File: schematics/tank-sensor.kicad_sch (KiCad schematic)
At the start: 32 parts, among them J10 Solar Panel, J8 Pressure Sensor, J9 Battery Connector, Q1 BS170, U1 ESP32-C6-DevKitC-1, U2 TSR_1-2450

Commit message: feat: Update component names
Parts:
- K1: value ~ -> EC2-12NU
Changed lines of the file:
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@@
 			)
 		)
-		(property "Value" "~"
+		(property "Value" "EC2-12NU"
 			(at 184.15 79.3496 90)
 			(effects

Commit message: feat: More updates to schematics
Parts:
- removed H1, H2, H3, H4: ~, symbol Mechanical:MountingHole
- removed U2: (no value), symbol AW_Misc_Library:Adafruit_ADS1115_Module
- removed U3: (no value), symbol AW_Misc_Library:XL6009E1_DC-DC_Stepup_Converter
- removed U4: (no value), symbol AW_Misc_Library:SDLA12TA_SLA_Charge_Module
- removed U5: (no value), symbol AW_Misc_Library:Pimoroni_BME280_Module
- added J11: SDLA12TA Charge module, symbol Connector_Generic:Conn_02x02_Counter_Clockwise
- added J12: XL6009E1 DC-DC converter, symbol Connector_Generic:Conn_01x04
- added U3: BME280, Package_LGA:Bosch_LGA-8_2.5x2.5mm_P0.65mm_ClockwisePinNumbering, symbol Sensor:BME280
- added U4: ADS1115, 1085:MODULE_1085, symbol 1085:1085
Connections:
- net 3v3: now also U4.JP2_1 (VIN)
- net BATTERY+12: now also J11.BAT
- net BATTLEVEL_SENSE: now also U4.JP1_5 (A0)
- net BOOST24POS: now also J12.3 (Pin_3)
- net BOOST_SUPPLY: now also J12.1 (IN_+)
- net GND: now also J11.GND, J12.2 (Pin_2), J12.4 (Pin_4), U3.1 (GND), U4.JP2_2 (GND)
- net LDR_SENSE: now also U4.JP1_3 (A2)
- net PANEL_NEG: now also J11.GND
- net PANEL_POS: now also J11.VIN
- net PRESS_SENSE: now also U4.JP1_4 (A1)
- net SCL: now also U4.JP2_3 (SCL)
- net SDA: now also U4.JP2_4 (SDA)
- new net: U4.SH1 (SHIELD), U4.SH2 (SHIELD), U4.SH3 (SHIELD), U4.SH4 (SHIELD)
- no-connect marks 11 -> 8
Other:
- note removed: "24V supply and sensing for submersible pressure sensor"
- note removed: "Analogue to Digital Conversion"
- note removed: "Environment Monitor and Control"
- note removed: "Power Supply"
- note removed: "Power control for 24V boost converter power supply"
- moved on the sheet: D1, D2, J1, J10, J2, J3, J4, J5, J6, J7, J8, J9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

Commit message: feat:Connected all the parts in the schematic
Almost complete, need to verify numbers for resistors
and diodes

#3
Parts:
- removed U3: BME280, Package_LGA:Bosch_LGA-8_2.5x2.5mm_P0.65mm_ClockwisePinNumbering, symbol Sensor:BME280
- added J13: BME280 3.3V, symbol Connector_Generic:Conn_01x06
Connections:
- net 3v3: now also U1.1 (3V3), J13.6 (Pin_6)
- net BATTLEVEL_SENSE: now also U4.JP1_2 (A3); no longer U4.JP1_5 (A0)
- net BOOST_ENABLE: now also U1.23 (GPIO18)
- net GND: now also J13.5 (Pin_5)
- net LDR_SENSE: now also U4.JP1_5 (A0); no longer U4.JP1_3 (A2)
- net OFFLINE_MODE: now also U1.28 (GPIO23)
- net SCL: now also U1.11 (GPIO11), J13.4 (Pin_4)
- net SDA: now also U1.10 (GPIO10), J13.3 (Pin_3)
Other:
- moved on the sheet: D1, R1, R2, R4, R7, SW1, U1, U4

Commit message: Just in case
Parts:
- removed D2: ~, symbol Device:D
- added D3: 1N4007, Diode_THT:D_DO-41_SOD81_P10.16mm_Horizontal, symbol Diode:1N4007
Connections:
- net BATTERY+12: now also D3.1 (K)
- net BOOST_SWITCH: now also D3.2 (A)
- no-connect marks 8 -> 38
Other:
- note added: "mosfet"
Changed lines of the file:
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@@
 	)
 	(no_connect
+		(at 63.5 97.79)
+	)
+	(no_connect
+		(at 33.02 90.17)
+	)
+	(no_connect
 		(at 73.66 30.48)
 	)
@@
 	)
 	(no_connect
+		(at 137.16 124.46)
+	)
+	(no_connect
+		(at 63.5 105.41)
+	)
+	(no_connect
+		(at 137.16 144.78)
+	)
+	(no_connect
+		(at 86.36 129.54)
+	)
+	(no_connect
 		(at 261.62 72.39)
 	)
 	(no_connect
+		(at 33.02 95.25)
+	)
+	(no_connect
+		(at 137.16 129.54)
+	)
+	(no_connect
+		(at 86.36 132.08)
+	)
+	(no_connect
+		(at 137.16 127)
+	)
+	(no_connect
+		(at 137.16 142.24)
+	)
+	(no_connect
+		(at 86.36 154.94)
+	)
+	(no_connect
+		(at 137.16 134.62)
+	)
+	(no_connect
+		(at 137.16 132.08)
+	)
+	(no_connect
+		(at 137.16 157.48)
+	)
+	(no_connect
+		(at 33.02 102.87)
+	)
+	(no_connect
+		(at 86.36 147.32)
+	)
+	(no_connect
+		(at 82.55 177.8)
+	)
+	(no_connect
+		(at 86.36 144.78)
+	)
+	(no_connect
 		(at 161.29 35.56)
 	)
 	(no_connect
+		(at 82.55 180.34)
+	)
+	(no_connect
+		(at 86.36 139.7)
+	)
+	(no_connect
+		(at 137.16 154.94)
+	)
+	(no_connect
+		(at 86.36 152.4)
+	)
+	(no_connect
 		(at 261.62 69.85)
 	)
 	(no_connect
+		(at 86.36 124.46)
+	)
+	(no_connect
 		(at 31.75 22.86)
 	)
 	(no_connect
+		(at 86.36 142.24)
+	)
+	(no_connect
+		(at 44.45 22.86)
+	)
+	(no_connect
+		(at 63.5 92.71)
+	)
+	(no_connect
 		(at 161.29 25.4)
 	)
 	(no_connect
-		(at 46.99 20.32)
+		(at 86.36 149.86)
+	)
+	(no_connect
+		(at 137.16 139.7)
+	)
+	(no_connect
+		(at 137.16 152.4)
+	)
+	(no_connect
+		(at 137.16 147.32)
 	)
 	(wire
@@
 	(wire
 		(pts
-			(xy 172.72 55.88) (xy 179.07 55.88)
+			(xy 172.72 59.69) (xy 179.07 59.69)
 		)
 		(stroke
@@
 	(wire
 		(pts
-			(xy 158.75 43.18) (xy 158.75 55.88)
+			(xy 158.75 43.18) (xy 158.75 59.69)
 		)
 		(stroke
@@
 	(wire
 		(pts
-			(xy 158.75 55.88) (xy 165.1 55.88)
+			(xy 158.75 59.69) (xy 165.1 59.69)
 		)
 		(stroke
@@
 	(wire
 		(pts
-			(xy 179.07 55.88) (xy 179.07 43.18)
+			(xy 179.07 59.69) (xy 179.07 43.18)
 		)
 		(stroke
@@
 		)
 	)
+	(text "mosfet"
+		(exclude_from_sim no)
+		(at 189.23 79.756 0)
+		(effects
+			(font
+				(size 1.27 1.27)
+			)
+		)
+	)
 	(text "This is intended as a green LED\n with 2V drop and 15mA."
 		(exclude_from_sim no)
@@
 		)
 	)
-	(global_label "3v3"
-		(shape input)
-		(at 127 176.53 180)
-		(fields_autoplaced yes)
-		(effects
-			(font
-				(size 1.27 1.27)
-			)
-			(justify right)
-		)
-		(property "Intersheetrefs" "${INTERSHEET_REFS}"
-			(at 120.6282 176.53 0)
-			(effects
-				(font
-					(size 1.27 1.27)
-				)
-				(justify right)
-				(hide yes)
-			)
-		)
-	)
 	(global_label "BATTERY+12"
 		(shape input)
@@
 	(global_label "CONSOLE_RX"
 		(shape input)
-		(at 168.91 118.11 0)
+		(at 171.45 125.73 0)
 		(fields_autoplaced yes)
 		(effects
@@
 		)
 		(property "Intersheetrefs" "${INTERSHEET_REFS}"
-			(at 183.9904 118.11 0)
+			(at 186.5304 125.73 0)
 			(effects
 				(font
@@
 		(dnp no)
 		(property "Reference" "K1"
-			(at 168.91 52.5018 90)
+			(at 169.164 14.224 90)
 			(effects
 				(font
@@
 		)
 		(property "Value" "EC2-12NU"
-			(at 168.91 50.1904 90)
+			(at 168.91 16.256 90)
 			(effects
 				(font
@@
 	)
 	(symbol
-		(lib_id "Device:D")
-		(at 168.91 55.88 0)
-		(unit 1)
-		(exclude_from_sim no)
-		(in_bom yes)
-		(on_board yes)
-		(dnp no)
-		(property "Reference" "D2"
-			(at 168.91 61.3918 0)
-			(effects
-				(font
-					(size 1.27 1.27)
-				)
-			)
-		)
-		(property "Value" "~"
-			(at 168.91 59.0804 0)
-			(effects
-				(font
-					(size 1.27 1.27)
-				)
-			)
-		)
-		(property "Footprint" ""
-			(at 168.91 55.88 0)
-			(effects
-				(font
-					(size 1.27 1.27)
-				)
-				(hide yes)
-			)
-		)
-		(property "Datasheet" "~"
-			(at 168.91 55.88 0)
-			(effects
-				(font
-					(size 1.27 1.27)
-				)
-				(hide yes)
-			)
-		)
-		(property "Description" ""
-			(at 168.91 55.88 0)
-			(effects
-				(font
-					(size 1.27 1.27)
-				)
-				(hide yes)
-			)
-		)
-		(pin "1"
-		)
-		(pin "2"
-		)
-		(instances
-			(project "tank-sensor"
-				(path "/a113f251-aa94-483d-8b1b-4a797e2f25c2"
-					(reference "D2")
-					(unit 1)
-				)
-			)
-		)
-	)
-	(symbol
 		(lib_id "power:GND")
 		(at 25.4 129.54 180)
@@
 					(unit 1)
 				)
+			)
+		)
+	)
+	(symbol
+		(lib_id "Diode:1N4007")
+		(at 168.91 59.69 0)
+		(unit 1)
+		(exclude_from_sim no)
+		(in_bom yes)
+		(on_board yes)
+		(dnp no)
+		(fields_autoplaced yes)
+		(property "Reference" "D3"
+			(at 168.91 53.34 0)
+			(effects
+				(font
+					(size 1.27 1.27)
+				)
+			)
+		)
+		(property "Value" "1N4007"
+			(at 168.91 55.88 0)
+			(effects
+				(font
+					(size 1.27 1.27)
+				)
+			)
+		)
+		(property "Footprint" "Diode_THT:D_DO-41_SOD81_P10.16mm_Horizontal"
+			(at 168.91 64.135 0)
+			(effects
+				(font
+					(size 1.27 1.27)
+				)
+				(hide yes)
+			)
+		)
+		(property "Datasheet" "http://www.vishay.com/docs/88503/1n4001.pdf"
+			(at 168.91 59.69 0)
+			(effects
+				(font
+					(size 1.27 1.27)
+				)
+				(hide yes)
+			)
+		)
+		(property "Description" "1000V 1A General Purpose Rectifier Diode, DO-41"
+			(at 168.91 59.69 0)
+			(effects
+				(font
+					(size 1.27 1.27)
+				)
+				(hide yes)
+			)
+		)
+		(property "Sim.Device" "D"
+			(at 168.91 59.69 0)
+			(effects
+				(font
+					(size 1.27 1.27)
+				)
+				(hide yes)
+			)
+		)
+		(property "Sim.Pins" "1=K 2=A"
+			(at 168.91 59.69 0)
+			(effects
+				(font
+					(size 1.27 1.27)
+				)
+				(hide yes)
+			)
+		)
+		(pin "2"
+		)
+		(pin "1"
+		)
+		(instances
+			(project ""
+				(path "/a113f251-aa94-483d-8b1b-4a797e2f25c2"
+					(reference "D3")
+					(unit 1)
+				)

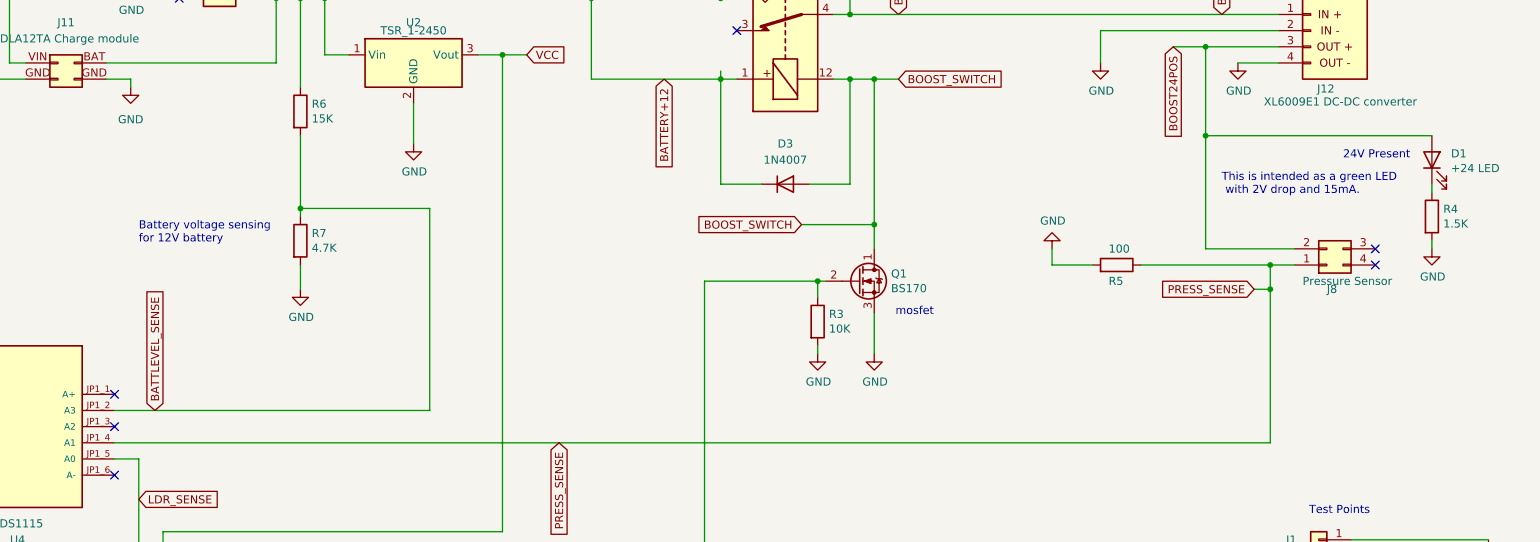
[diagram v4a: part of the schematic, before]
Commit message: Add the ability to measure the pressure sensor voltage
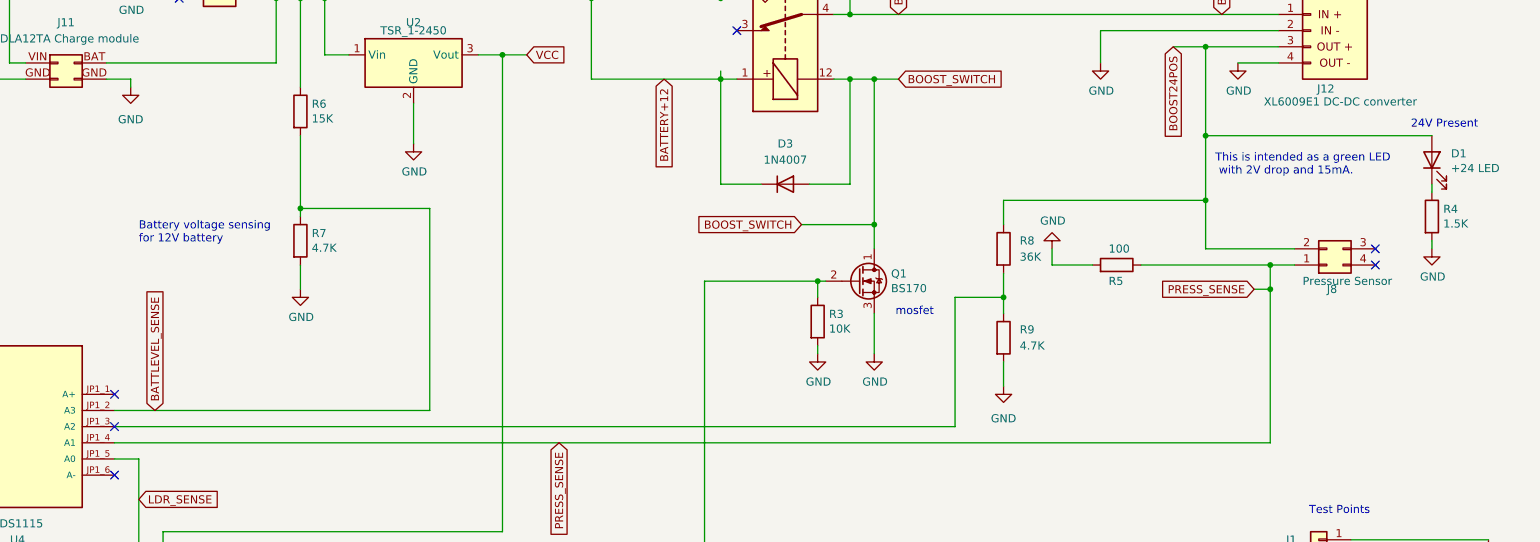
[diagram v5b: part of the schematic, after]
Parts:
- added R8: 36K, symbol Device:R
- added R9: 4.7K, symbol Device:R
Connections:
- net BOOST24POS: now also R8.1
- net GND: now also R9.2
- net at U4.JP1_3 (A2): now also R8.2, R9.1

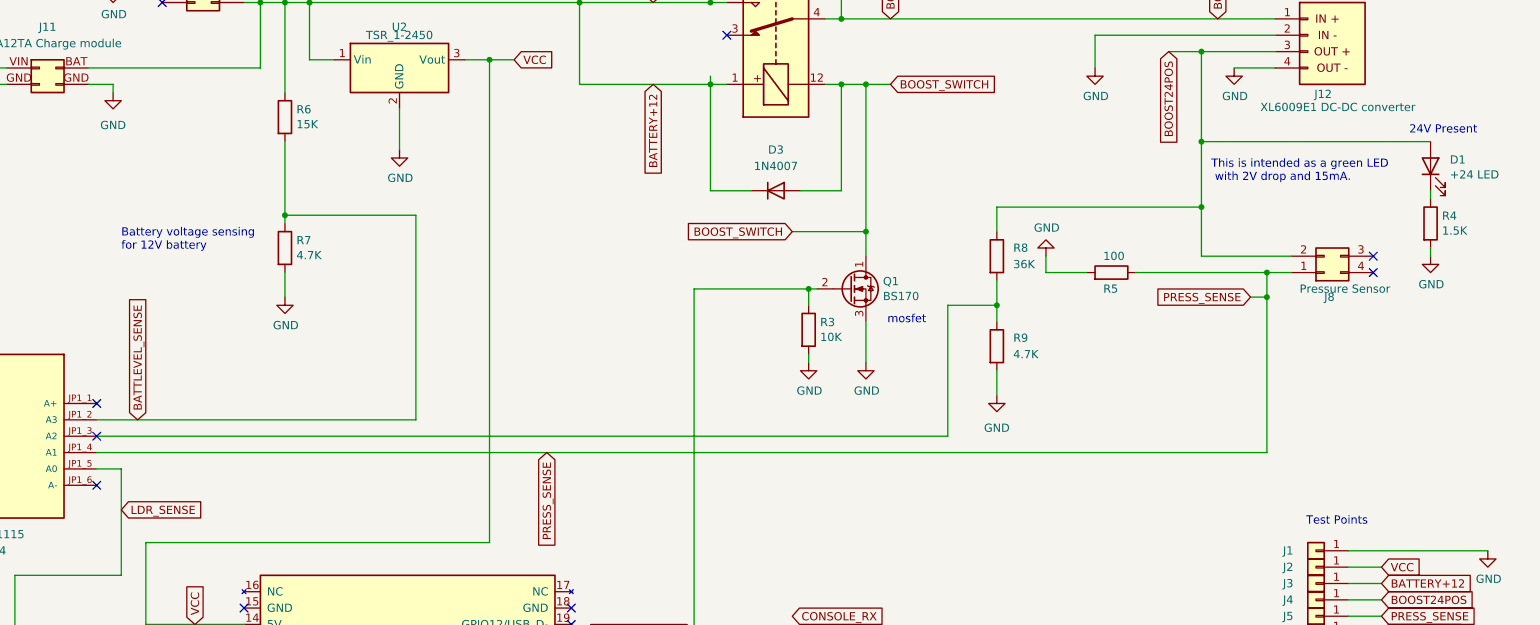
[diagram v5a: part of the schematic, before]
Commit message: Add reading the ADS1115 analog-digital converter
This also requires making changes to the different voltage
divider resistors.
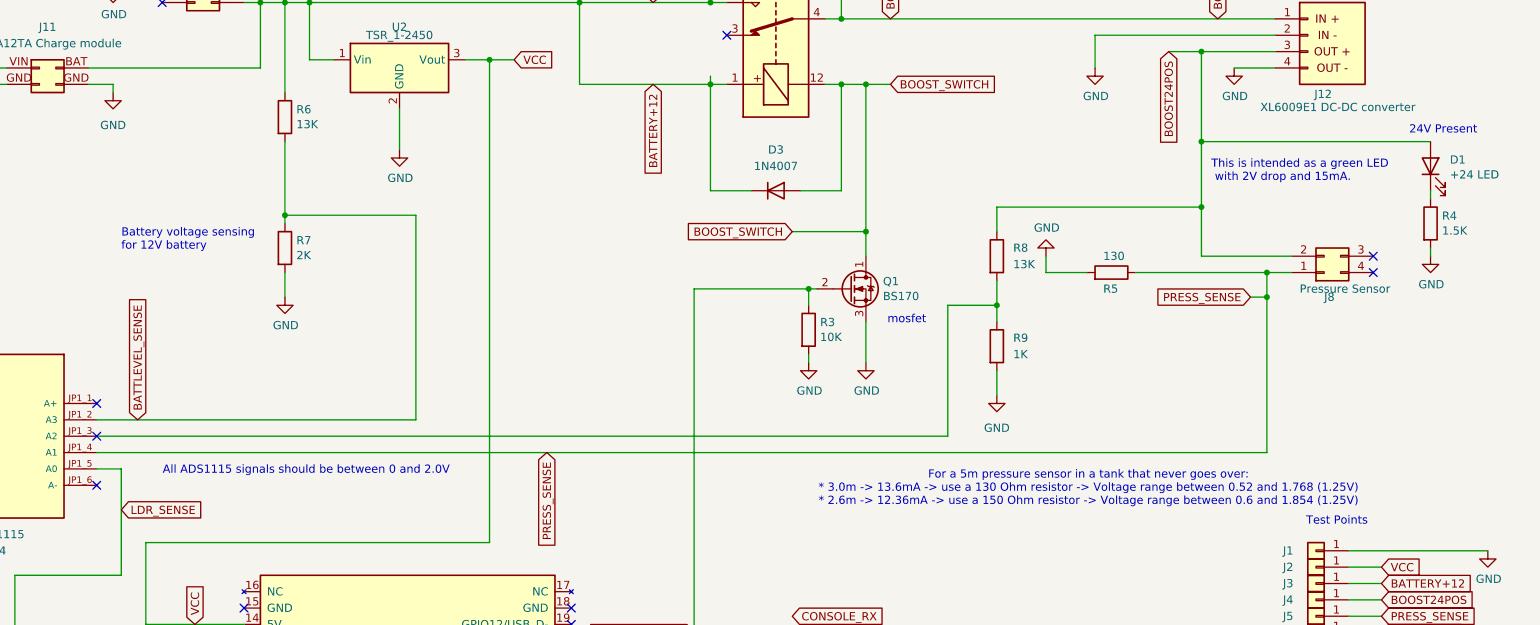
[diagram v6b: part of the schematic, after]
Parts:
- R5: value 100 -> 130
- R6: value 15K -> 13K
- R7: value 4.7K -> 2K
- R8: value 36K -> 13K
- R9: value 4.7K -> 1K
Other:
- note added: "All ADS1115 signals should be between 0 and 2.0V"
- note added: "For a 5m pressure sensor in a tank that never goes over: * 3.0m -> 13.6mA -> use a 130 Ohm resistor -> Voltage range between 0.52 and 1.768 (1.25V) * 2.6m -> 12.36mA -> use a 150 Ohm resistor -> Voltage range between 0.6 and 1.854 (1.25V)"
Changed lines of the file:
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@@
 		)
 	)
+	(text "All ADS1115 signals should be between 0 and 2.0V"
+		(exclude_from_sim no)
+		(at 96.012 103.124 0)
+		(effects
+			(font
+				(size 1.27 1.27)
+			)
+		)
+	)
 	(text "Battery voltage sensing \nfor 12V battery"
 		(exclude_from_sim no)
@@
 		)
 	)
+	(text "For a 5m pressure sensor in a tank that never goes over:\n* 3.0m -> 13.6mA -> use a 130 Ohm resistor -> Voltage range between 0.52 and 1.768 (1.25V)\n* 2.6m -> 12.36mA -> use a 150 Ohm resistor -> Voltage range between 0.6 and 1.854 (1.25V)"
+		(exclude_from_sim no)
+		(at 217.424 105.918 0)
+		(effects
+			(font
+				(size 1.27 1.27)
+			)
+		)
+	)
 	(text "Close this jumper for offline operation.\nThis suppresses LoRaWAN connectivity."
 		(exclude_from_sim no)
@@
 			)
 		)
-		(property "Value" "4.7K"
+		(property "Value" "1K"
 			(at 205.74 85.0899 0)
 			(effects
@@
 			)
 		)
-		(property "Value" "4.7K"
+		(property "Value" "2K"
 			(at 94.488 69.723 0)
 			(effects
@@
 			)
 		)
-		(property "Value" "15K"
+		(property "Value" "13K"
 			(at 94.488 49.403 0)
 			(effects
@@
 			)
 		)
-		(property "Value" "36K"
+		(property "Value" "13K"
 			(at 205.74 71.1199 0)
 			(effects
@@
 			)
 		)
-		(property "Value" "100"
+		(property "Value" "130"
 			(at 219.71 69.85 90)
 			(effects
